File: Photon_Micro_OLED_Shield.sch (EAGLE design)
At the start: 26 parts

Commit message: qc fixes
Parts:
- C1: device SparkFun-Passives:CAP0805 -> SparkFun-Capacitors:2.2UF-25V-+80/-20(0805)
- C2, C3: value 1uF X5R -> 1uF; device SparkFun-Passives:CAP0805 -> SparkFun-Capacitors:1UF-25V-10%(0805)"
- C4, C6: PROD_ID (none) -> CAP-00868
- C5: value 4.7uF/16V -> 4.7uF; device SparkFun-Passives:CAP1206 -> SparkFun-Capacitors:4.7UF-16V-20%,+80%-(1206); PROD_ID (none) -> CAP-10300
- OLED1: PROD_ID (none) -> LCD-12019
- R1: PROD_ID (none) -> RES-12024
- R2: PROD_ID (none) -> RES-00824
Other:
- moved on the sheet: JP3

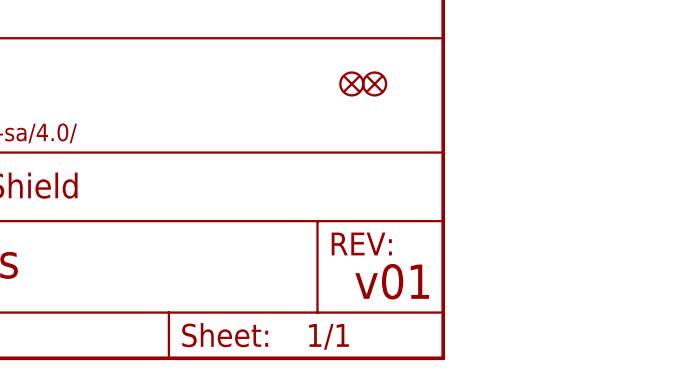
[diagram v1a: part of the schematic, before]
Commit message: new design
moved screen to top and extended board so it will work better with the
rest of the photon shields
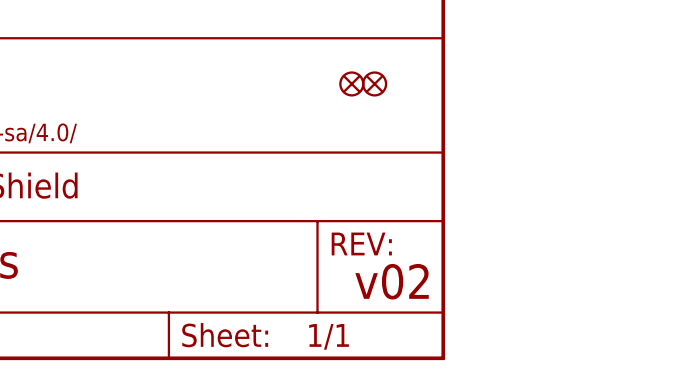
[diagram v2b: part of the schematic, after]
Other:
- note added: "v02"
- note removed: "v01"
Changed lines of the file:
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@@
 <grid distance="0.1" unitdist="inch" unit="inch" style="lines" multiple="1" display="no" altdistance="0.01" altunitdist="inch" altunit="inch"/>
 <layers>
-<layer number="1" name="Top" color="4" fill="1" visible="yes" active="no"/>
-<layer number="2" name="Route2" color="1" fill="3" visible="yes" active="no"/>
-<layer number="3" name="Route3" color="4" fill="3" visible="yes" active="no"/>
-<layer number="4" name="Route4" color="1" fill="4" visible="yes" active="no"/>
-<layer number="5" name="Route5" color="4" fill="4" visible="yes" active="no"/>
-<layer number="6" name="Route6" color="1" fill="8" visible="yes" active="no"/>
-<layer number="7" name="Route7" color="4" fill="8" visible="yes" active="no"/>
-<layer number="8" name="Route8" color="1" fill="2" visible="yes" active="no"/>
-<layer number="9" name="Route9" color="4" fill="2" visible="yes" active="no"/>
-<layer number="10" name="Route10" color="1" fill="7" visible="yes" active="no"/>
-<layer number="11" name="Route11" color="4" fill="7" visible="yes" active="no"/>
-<layer number="12" name="Route12" color="1" fill="5" visible="yes" active="no"/>
-<layer number="13" name="Route13" color="4" fill="5" visible="yes" active="no"/>
-<layer number="14" name="Route14" color="1" fill="6" visible="yes" active="no"/>
-<layer number="15" name="Route15" color="4" fill="6" visible="yes" active="no"/>
-<layer number="16" name="Bottom" color="1" fill="1" visible="yes" active="no"/>
-<layer number="17" name="Pads" color="2" fill="1" visible="yes" active="no"/>
-<layer number="18" name="Vias" color="2" fill="1" visible="yes" active="no"/>
-<layer number="19" name="Unrouted" color="6" fill="1" visible="yes" active="no"/>
-<layer number="20" name="Dimension" color="15" fill="1" visible="yes" active="no"/>
-<layer number="21" name="tPlace" color="16" fill="1" visible="yes" active="no"/>
-<layer number="22" name="bPlace" color="14" fill="1" visible="yes" active="no"/>
-<layer number="23" name="tOrigins" color="15" fill="1" visible="yes" active="no"/>
-<layer number="24" name="bOrigins" color="15" fill="1" visible="yes" active="no"/>
-<layer number="25" name="tNames" color="7" fill="1" visible="yes" active="no"/>
-<layer number="26" name="bNames" color="7" fill="1" visible="yes" active="no"/>
-<layer number="27" name="tValues" color="7" fill="1" visible="yes" active="no"/>
-<layer number="28" name="bValues" color="7" fill="1" visible="yes" active="no"/>
+<layer number="1" name="Top" color="4" fill="1" visible="no" active="no"/>
+<layer number="2" name="Route2" color="1" fill="3" visible="no" active="no"/>
+<layer number="3" name="Route3" color="4" fill="3" visible="no" active="no"/>
+<layer number="4" name="Route4" color="1" fill="4" visible="no" active="no"/>
+<layer number="5" name="Route5" color="4" fill="4" visible="no" active="no"/>
+<layer number="6" name="Route6" color="1" fill="8" visible="no" active="no"/>
+<layer number="7" name="Route7" color="4" fill="8" visible="no" active="no"/>
+<layer number="8" name="Route8" color="1" fill="2" visible="no" active="no"/>
+<layer number="9" name="Route9" color="4" fill="2" visible="no" active="no"/>
+<layer number="10" name="Route10" color="1" fill="7" visible="no" active="no"/>
+<layer number="11" name="Route11" color="4" fill="7" visible="no" active="no"/>
+<layer number="12" name="Route12" color="1" fill="5" visible="no" active="no"/>
+<layer number="13" name="Route13" color="4" fill="5" visible="no" active="no"/>
+<layer number="14" name="Route14" color="1" fill="6" visible="no" active="no"/>
+<layer number="15" name="Route15" color="4" fill="6" visible="no" active="no"/>
+<layer number="16" name="Bottom" color="1" fill="1" visible="no" active="no"/>
+<layer number="17" name="Pads" color="2" fill="1" visible="no" active="no"/>
+<layer number="18" name="Vias" color="2" fill="1" visible="no" active="no"/>
+<layer number="19" name="Unrouted" color="6" fill="1" visible="no" active="no"/>
+<layer number="20" name="Dimension" color="15" fill="1" visible="no" active="no"/>
+<layer number="21" name="tPlace" color="16" fill="1" visible="no" active="no"/>
+<layer number="22" name="bPlace" color="14" fill="1" visible="no" active="no"/>
+<layer number="23" name="tOrigins" color="15" fill="1" visible="no" active="no"/>
+<layer number="24" name="bOrigins" color="15" fill="1" visible="no" active="no"/>
+<layer number="25" name="tNames" color="7" fill="1" visible="no" active="no"/>
+<layer number="26" name="bNames" color="7" fill="1" visible="no" active="no"/>
+<layer number="27" name="tValues" color="7" fill="1" visible="no" active="no"/>
+<layer number="28" name="bValues" color="7" fill="1" visible="no" active="no"/>
 <layer number="29" name="tStop" color="7" fill="3" visible="no" active="no"/>
 <layer number="30" name="bStop" color="7" fill="6" visible="no" active="no"/>
@@
 <layer number="35" name="tGlue" color="7" fill="4" visible="no" active="no"/>
 <layer number="36" name="bGlue" color="7" fill="5" visible="no" active="no"/>
-<layer number="37" name="tTest" color="7" fill="1" visible="yes" active="no"/>
-<layer number="38" name="bTest" color="7" fill="1" visible="yes" active="no"/>
+<layer number="37" name="tTest" color="7" fill="1" visible="no" active="no"/>
+<layer number="38" name="bTest" color="7" fill="1" visible="no" active="no"/>
 <layer number="39" name="tKeepout" color="4" fill="11" visible="no" active="no"/>
 <layer number="40" name="bKeepout" color="1" fill="11" visible="no" active="no"/>
@@
 <layer number="44" name="Drills" color="7" fill="1" visible="no" active="no"/>
 <layer number="45" name="Holes" color="7" fill="1" visible="no" active="no"/>
-<layer number="46" name="Milling" color="3" fill="1" visible="yes" active="no"/>
-<layer number="47" name="Measures" color="7" fill="1" visible="yes" active="no"/>
-<layer number="48" name="Document" color="7" fill="1" visible="yes" active="no"/>
-<layer number="49" name="Reference" color="7" fill="1" visible="yes" active="no"/>
-<layer number="50" name="dxf" color="7" fill="1" visible="yes" active="no"/>
-<layer number="51" name="tDocu" color="6" fill="1" visible="yes" active="no"/>
-<layer number="52" name="bDocu" color="7" fill="1" visible="yes" active="no"/>
-<layer number="53" name="tGND_GNDA" color="7" fill="1" visible="yes" active="no"/>
-<layer number="54" name="bGND_GNDA" color="7" fill="1" visible="yes" active="no"/>
-<layer number="56" name="wert" color="7" fill="1" visible="yes" active="no"/>
-<layer number="57" name="tCAD" color="7" fill="1" visible="yes" active="no"/>
-<layer number="59" name="tCarbon" color="7" fill="1" visible="yes" active="no"/>
-<layer number="60" name="bCarbon" color="7" fill="1" visible="yes" active="no"/>
+<layer number="46" name="Milling" color="3" fill="1" visible="no" active="no"/>
+<layer number="47" name="Measures" color="7" fill="1" visible="no" active="no"/>
+<layer number="48" name="Document" color="7" fill="1" visible="no" active="no"/>
+<layer number="49" name="Reference" color="7" fill="1" visible="no" active="no"/>
+<layer number="50" name="dxf" color="7" fill="1" visible="no" active="no"/>
+<layer number="51" name="tDocu" color="6" fill="1" visible="no" active="no"/>
+<layer number="52" name="bDocu" color="7" fill="1" visible="no" active="no"/>
+<layer number="53" name="tGND_GNDA" color="7" fill="1" visible="no" active="no"/>
+<layer number="54" name="bGND_GNDA" color="7" fill="1" visible="no" active="no"/>
+<layer number="56" name="wert" color="7" fill="1" visible="no" active="no"/>
+<layer number="57" name="tCAD" color="7" fill="1" visible="no" active="no"/>
+<layer number="59" name="tCarbon" color="7" fill="1" visible="no" active="no"/>
+<layer number="60" name="bCarbon" color="7" fill="1" visible="no" active="no"/>
 <layer number="90" name="Modules" color="5" fill="1" visible="yes" active="yes"/>
 <layer number="91" name="Nets" color="2" fill="1" visible="yes" active="yes"/>
@@
 <sheet>
 <plain>
-<text x="239.014" y="6.604" size="3.81" layer="94">v01</text>
+<text x="239.014" y="6.604" size="3.81" layer="94">v02</text>
 <text x="165.1" y="8.89" size="3.81" layer="94">Ben Leduc-Mills</text>
 <text x="153.416" y="153.416" size="1.778" layer="97">1.65 &lt;= VDD &lt;= 3.3</text>

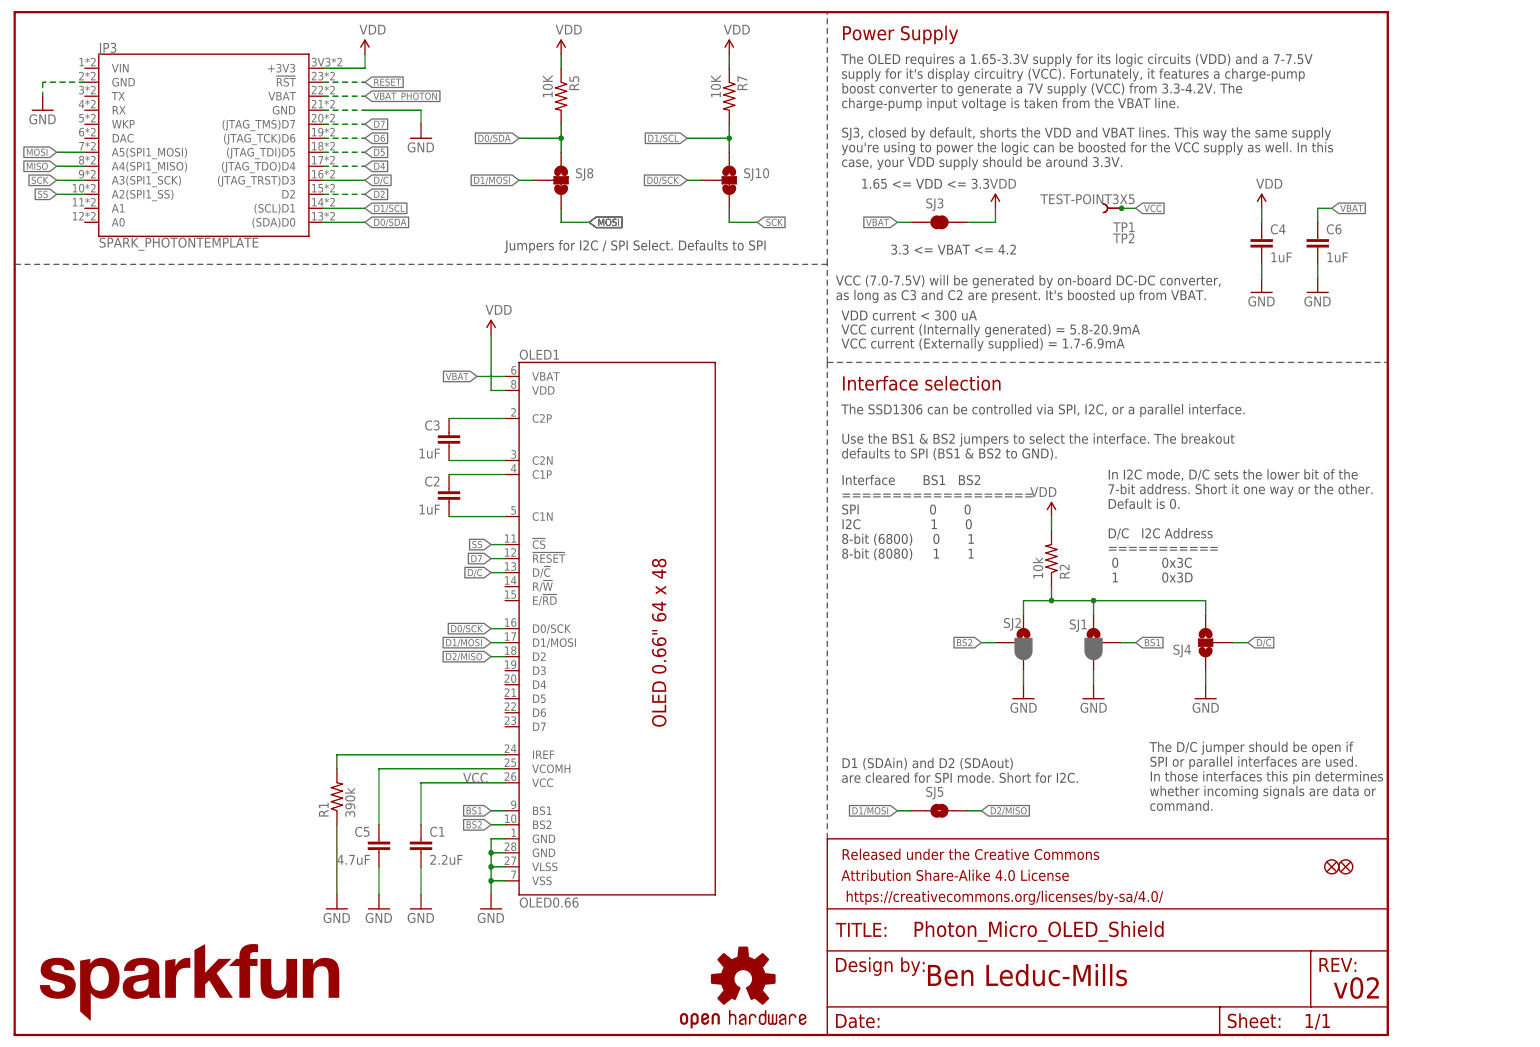
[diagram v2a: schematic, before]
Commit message: Adding gap between Photon and pin-break outs. Moving D/C to pin D6.
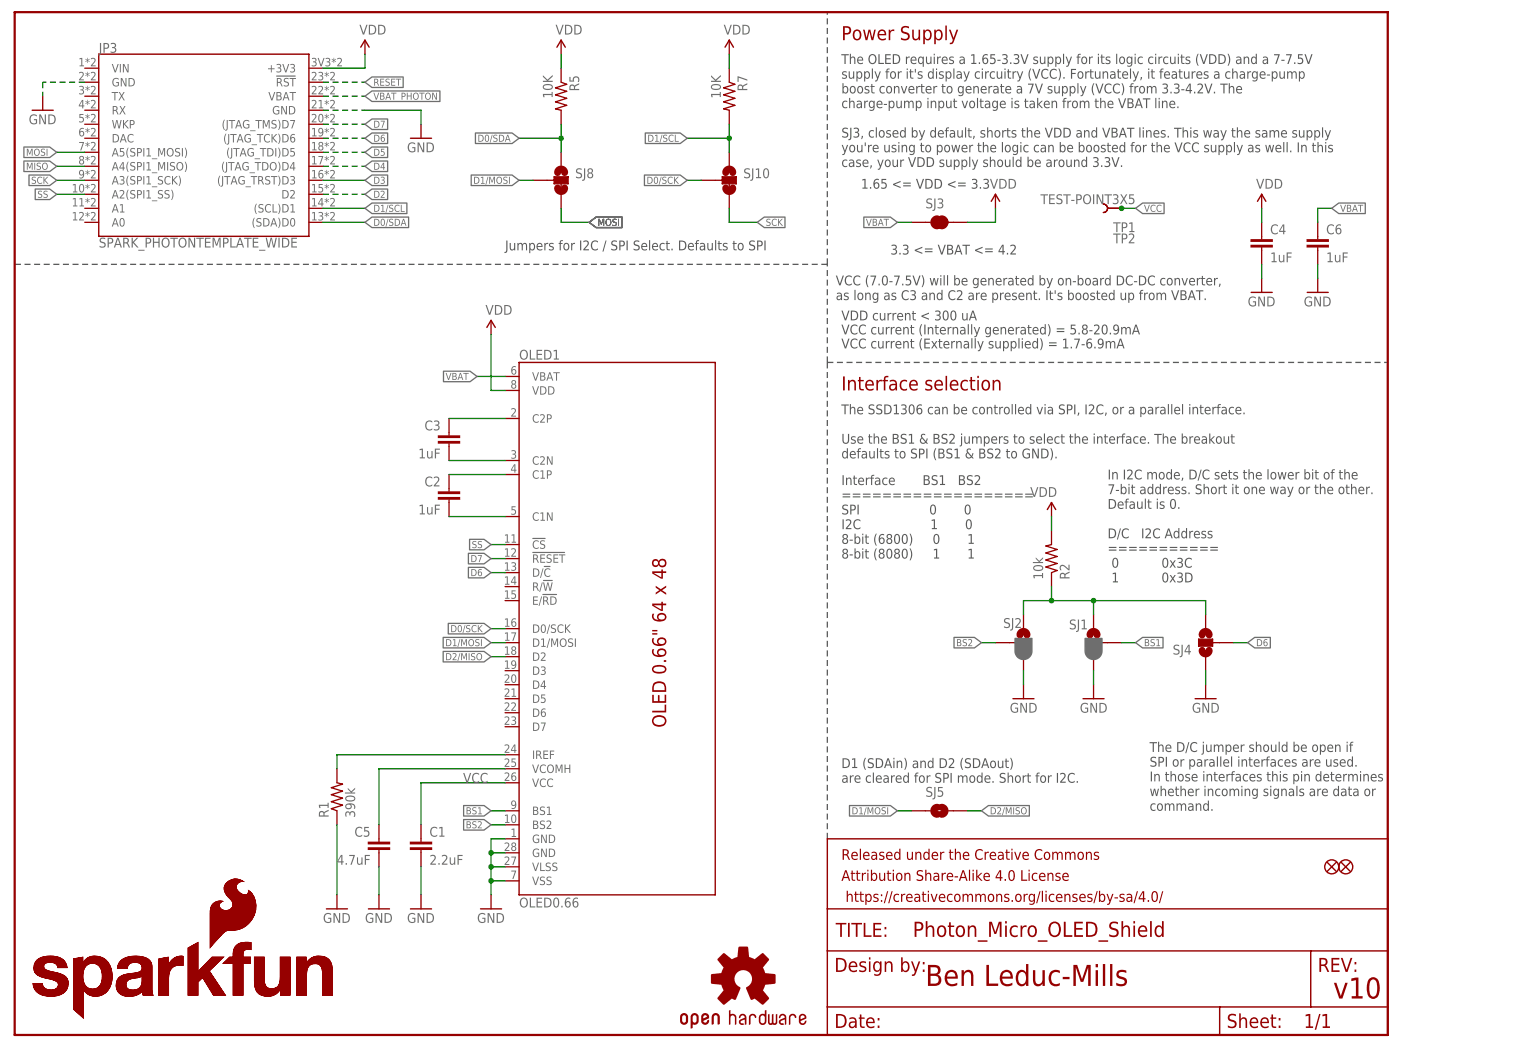
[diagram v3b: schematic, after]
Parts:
- added LOGO2: SFE_LOGO_NAME_FLAME.1_INCH, SparkFun-Aesthetics:SFE_LOGO_NAME_FLAME.1_INCH
- JP3: value SPARK_PHOTONTEMPLATE -> SPARK_PHOTONTEMPLATE_WIDE; device template_temp:SPARK_PHOTONTEMPLATE -> template_temp:SPARK_PHOTONTEMPLATE_WIDE
- LOGO1: value SFE_LOGO_NAME.1_INCH -> SFE_LOGO_NAME_FLAME.1_INCH; device SparkFun-Aesthetics:SFE_LOGO_NAME.1_INCH -> SparkFun-Aesthetics:SFE_LOGO_NAME_FLAME.1_INCH
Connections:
- removed net D/C: JP3.(JTAG_TRST)D3, OLED1.D/!C!, SJ4.2
- new net D3: JP3.(JTAG_TRST)D3
- net D6: now also OLED1.D/!C!, SJ4.2
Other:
- note added: "v10"
- note removed: "v02"
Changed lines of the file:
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@@
 <part name="GND11" library="SparkFun-Aesthetics" deviceset="GND" device=""/>
 <part name="LOGO3" library="SparkFun-Aesthetics" deviceset="OSHW-LOGO" device="S"/>
-<part name="JP3" library="template_temp" deviceset="SPARK_PHOTON" device="TEMPLATE"/>
+<part name="JP3" library="template_temp" deviceset="SPARK_PHOTON" device="TEMPLATE_WIDE" value="SPARK_PHOTONTEMPLATE_WIDE"/>
 <part name="GND10" library="SparkFun-Aesthetics" deviceset="GND" device=""/>
 <part name="GND12" library="SparkFun-Aesthetics" deviceset="GND" device=""/>
@@
 <part name="SJ10" library="SparkFun-Passives" deviceset="JUMPER-PAD-3-2OF3_NC_BY_TRACE" device="_SMALL" value=""/>
 <part name="SUPPLY9" library="SparkFun-Aesthetics" deviceset="VDD" device=""/>
-<part name="LOGO1" library="SparkFun-Aesthetics" deviceset="SFE_LOGO_NAME" device=".1_INCH"/>
 <part name="SJ4" library="SparkFun-Passives" deviceset="JUMPER-PAD-3-NO" device="YES_SILK" value=""/>
 <part name="SUPPLY5" library="SparkFun-Aesthetics" deviceset="VDD" device=""/>
+<part name="LOGO1" library="SparkFun-Aesthetics" deviceset="SFE_LOGO_NAME_FLAME" device=".1_INCH"/>
+<part name="LOGO2" library="SparkFun-Aesthetics" deviceset="SFE_LOGO_NAME_FLAME" device=".1_INCH"/>
 </parts>
 <sheets>
 <sheet>
 <plain>
-<text x="239.014" y="6.604" size="3.81" layer="94">v02</text>
+<text x="239.014" y="6.604" size="3.81" layer="94">v10</text>
 <text x="165.1" y="8.89" size="3.81" layer="94">Ben Leduc-Mills</text>
 <text x="153.416" y="153.416" size="1.778" layer="97">1.65 &lt;= VDD &lt;= 3.3</text>
@@
 <instance part="SJ10" gate="G$1" x="129.54" y="154.94"/>
 <instance part="SUPPLY9" gate="VDD" x="129.54" y="177.8"/>
-<instance part="LOGO1" gate="G$1" x="2.54" y="2.54"/>
 <instance part="SJ4" gate="G$1" x="215.9" y="71.12" rot="R180"/>
 <instance part="SUPPLY5" gate="VDD" x="63.5" y="177.8"/>
+<instance part="LOGO1" gate="G$1" x="2.54" y="2.54"/>
+<instance part="LOGO2" gate="G$1" x="2.54" y="2.54"/>
 </instances>
 <busses>
@@
 <label x="63.5" y="162.56" size="1.27" layer="95" ratio="12" xref="yes"/>
 </segment>
+<segment>
+<pinref part="OLED1" gate="G1" pin="D/!C!"/>
+<wire x1="88.9" y1="83.82" x2="86.36" y2="83.82" width="0.1524" layer="91"/>
+<label x="86.36" y="83.82" size="1.27" layer="95" rot="R180" xref="yes"/>
+</segment>
+<segment>
+<wire x1="220.98" y1="71.12" x2="223.52" y2="71.12" width="0.1524" layer="91"/>
+<label x="223.52" y="71.12" size="1.27" layer="95" xref="yes"/>
+<pinref part="SJ4" gate="G$1" pin="2"/>
+</segment>
 </net>
 <net name="D5" class="0">
@@
 </segment>
 </net>
-<net name="D/C" class="0">
+<net name="D2/MISO" class="0">
+<segment>
+<pinref part="OLED1" gate="G1" pin="D2"/>
+<wire x1="88.9" y1="68.58" x2="86.36" y2="68.58" width="0.1524" layer="91"/>
+<label x="86.36" y="68.58" size="1.27" layer="95" rot="R180" xref="yes"/>
+</segment>
+<segment>
+<pinref part="SJ5" gate="G$1" pin="2"/>
+<wire x1="172.72" y1="40.64" x2="175.26" y2="40.64" width="0.1524" layer="91"/>
+<label x="175.26" y="40.64" size="1.27" layer="95" xref="yes"/>
+</segment>
+</net>
+<net name="VBAT_PHOTON" class="0">
+<segment>
+<pinref part="JP3" gate="G$1" pin="VBAT"/>
+<wire x1="55.88" y1="170.18" x2="63.5" y2="170.18" width="0.1524" layer="91" style="longdash"/>
+<label x="63.5" y="170.18" size="1.27" layer="95" ratio="12" xref="yes"/>
+</segment>
+</net>
+<net name="D3" class="0">
 <segment>
 <pinref part="JP3" gate="G$1" pin="(JTAG_TRST)D3"/>
@@
 <label x="63.5" y="154.94" size="1.27" layer="95" xref="yes"/>
 </segment>
-<segment>
-<pinref part="OLED1" gate="G1" pin="D/!C!"/>
-<wire x1="88.9" y1="83.82" x2="86.36" y2="83.82" width="0.1524" layer="91"/>
-<label x="86.36" y="83.82" size="1.27" layer="95" rot="R180" xref="yes"/>
-</segment>
-<segment>
-<wire x1="220.98" y1="71.12" x2="223.52" y2="71.12" width="0.1524" layer="91"/>
-<label x="223.52" y="71.12" size="1.27" layer="95" xref="yes"/>
-<pinref part="SJ4" gate="G$1" pin="2"/>
-</segment>
-</net>
-<net name="D2/MISO" class="0">
-<segment>
-<pinref part="OLED1" gate="G1" pin="D2"/>
-<wire x1="88.9" y1="68.58" x2="86.36" y2="68.58" width="0.1524" layer="91"/>
-<label x="86.36" y="68.58" size="1.27" layer="95" rot="R180" xref="yes"/>
-</segment>
-<segment>
-<pinref part="SJ5" gate="G$1" pin="2"/>
-<wire x1="172.72" y1="40.64" x2="175.26" y2="40.64" width="0.1524" layer="91"/>
-<label x="175.26" y="40.64" size="1.27" layer="95" xref="yes"/>
-</segment>
-</net>
-<net name="VBAT_PHOTON" class="0">
-<segment>
-<pinref part="JP3" gate="G$1" pin="VBAT"/>
-<wire x1="55.88" y1="170.18" x2="63.5" y2="170.18" width="0.1524" layer="91" style="longdash"/>
-<label x="63.5" y="170.18" size="1.27" layer="95" ratio="12" xref="yes"/>
-</segment>
-</net>
+</net>
